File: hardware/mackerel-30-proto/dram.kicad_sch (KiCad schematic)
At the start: 8 parts, among them J11 Conn_02x05_Odd_Even, U10 SIMM72, U9 EPM7128, X3 CXO_DIP14

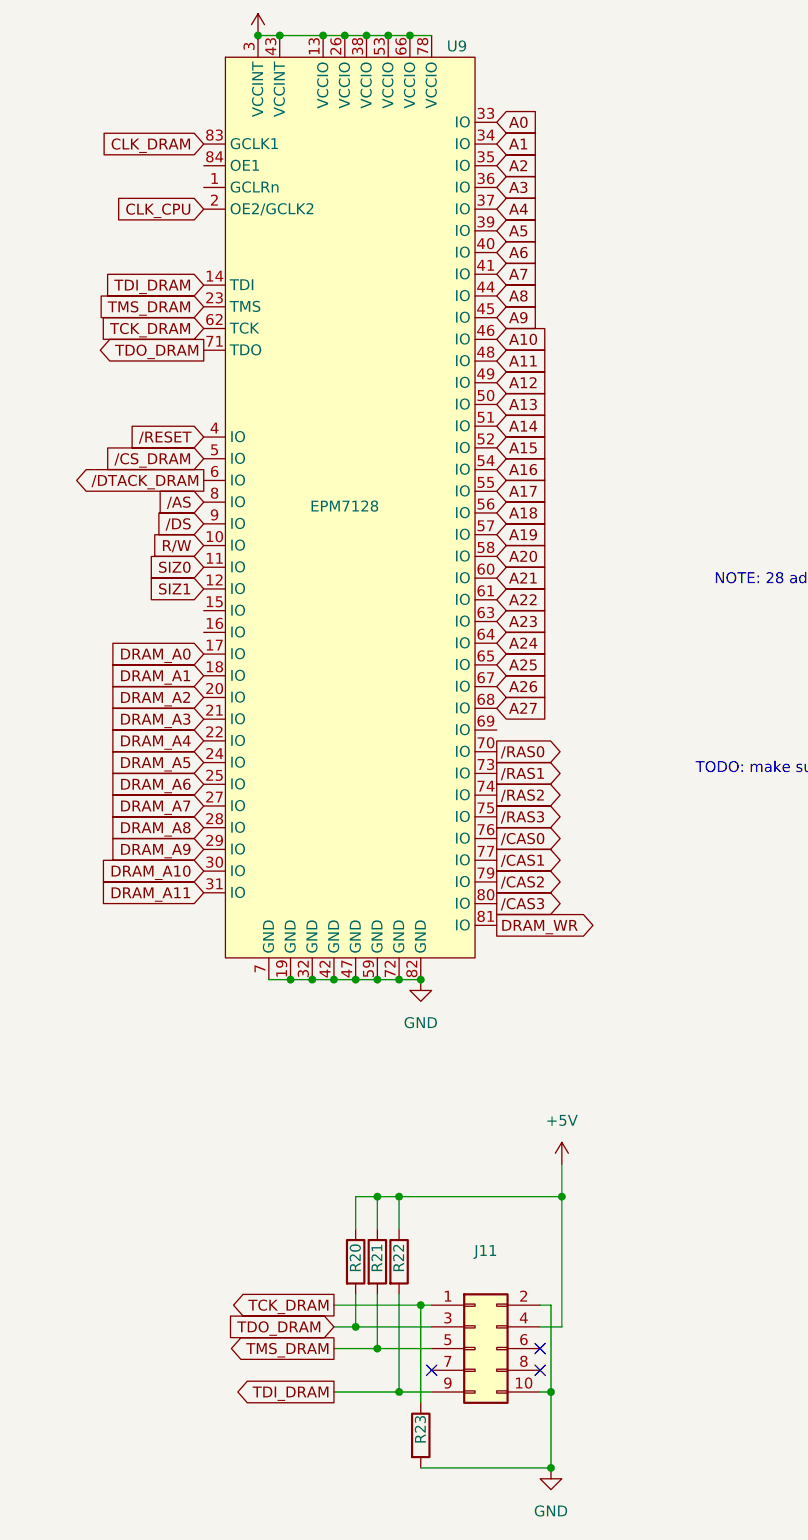
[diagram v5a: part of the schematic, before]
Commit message: rough layout of the PCB components
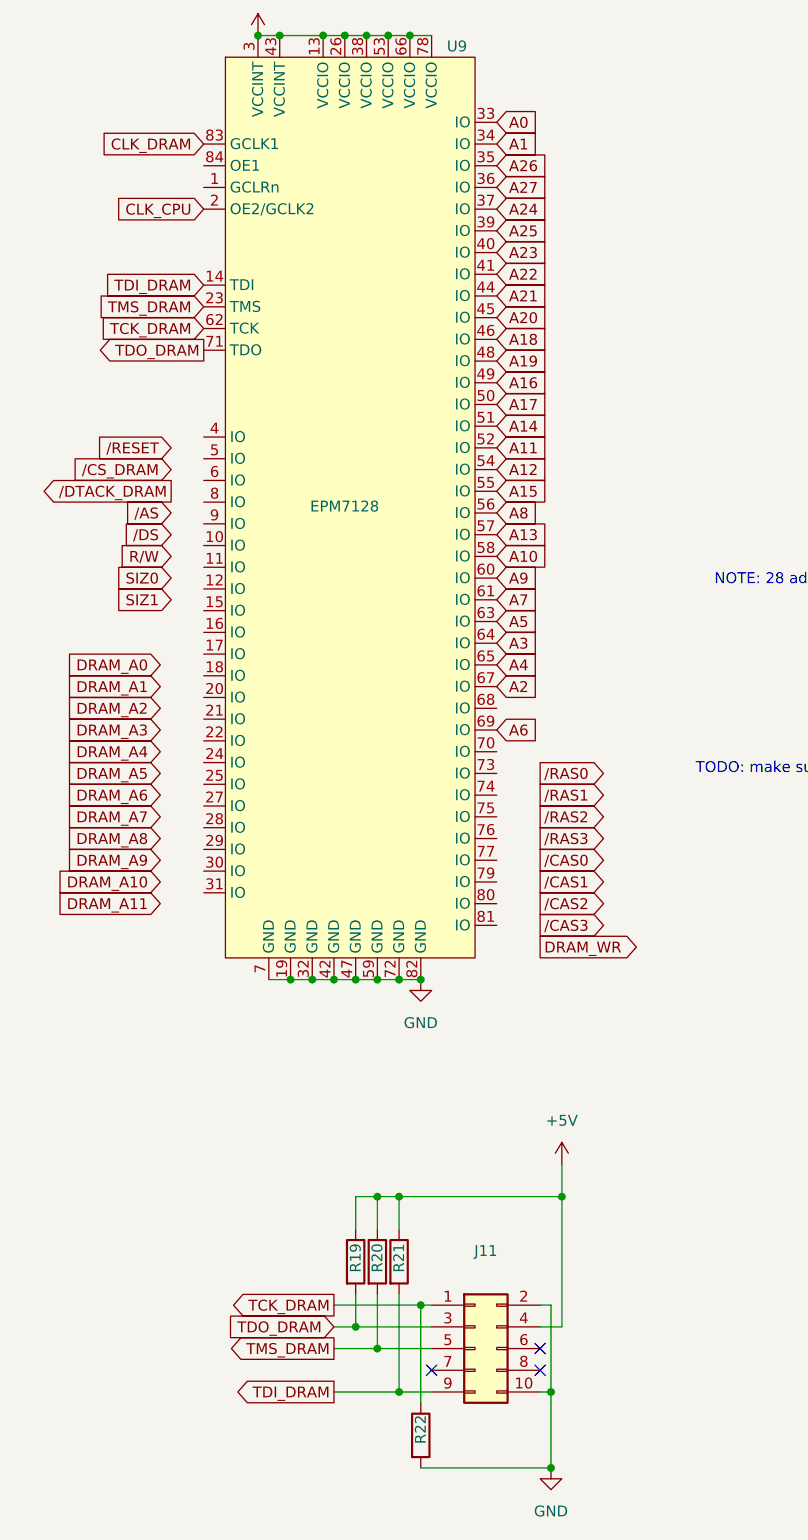
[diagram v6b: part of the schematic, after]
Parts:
- R19: renamed from R20; footprint Resistor_SMD:R_0805_2012Metric_Pad1.20x1.40mm_HandSolder -> Resistor_THT:R_Axial_DIN0207_L6.3mm_D2.5mm_P7.62mm_Horizontal
- R20: renamed from R21; footprint Resistor_SMD:R_0805_2012Metric_Pad1.20x1.40mm_HandSolder -> Resistor_THT:R_Axial_DIN0207_L6.3mm_D2.5mm_P7.62mm_Horizontal
- R21: renamed from R22; footprint Resistor_SMD:R_0805_2012Metric_Pad1.20x1.40mm_HandSolder -> Resistor_THT:R_Axial_DIN0207_L6.3mm_D2.5mm_P7.62mm_Horizontal
- R22: renamed from R23; footprint Resistor_SMD:R_0805_2012Metric_Pad1.20x1.40mm_HandSolder -> Resistor_THT:R_Axial_DIN0207_L6.3mm_D2.5mm_P7.62mm_Horizontal
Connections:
- net A10: now also U9.58 (IO); no longer U9.46 (IO)
- net A11: now also U9.52 (IO); no longer U9.48 (IO)
- net A12: now also U9.54 (IO); no longer U9.49 (IO)
- net A13: now also U9.57 (IO); no longer U9.50 (IO)
- net A15: now also U9.55 (IO); no longer U9.52 (IO)
- net A16: now also U9.49 (IO); no longer U9.54 (IO)
- net A17: now also U9.50 (IO); no longer U9.55 (IO)
- net A18: now also U9.46 (IO); no longer U9.56 (IO)
- net A19: now also U9.48 (IO); no longer U9.57 (IO)
- net A2: now also U9.67 (IO); no longer U9.35 (IO)
- net A20: now also U9.45 (IO); no longer U9.58 (IO)
- net A21: now also U9.44 (IO); no longer U9.60 (IO)
- net A22: now also U9.41 (IO); no longer U9.61 (IO)
- net A23: now also U9.40 (IO); no longer U9.63 (IO)
- net A24: now also U9.37 (IO); no longer U9.64 (IO)
- net A25: now also U9.39 (IO); no longer U9.65 (IO)
- net A26: now also U9.35 (IO); no longer U9.67 (IO)
- net A27: now also U9.36 (IO); no longer U9.68 (IO)
- net A3: now also U9.64 (IO); no longer U9.36 (IO)
- net A4: now also U9.65 (IO); no longer U9.37 (IO)
- net A5: now also U9.63 (IO); no longer U9.39 (IO)
- net A6: now also U9.69 (IO); no longer U9.40 (IO)
- net A7: now also U9.61 (IO); no longer U9.41 (IO)
- net A8: now also U9.56 (IO); no longer U9.44 (IO)
- net A9: now also U9.60 (IO); no longer U9.45 (IO)
- net DRAM_A0: no longer U9.17 (IO)
- net DRAM_A1: no longer U9.18 (IO)
- net DRAM_A10: no longer U9.30 (IO)
- net DRAM_A11: no longer U9.31 (IO)
- net DRAM_A2: no longer U9.20 (IO)
- net DRAM_A3: no longer U9.21 (IO)
- net DRAM_A4: no longer U9.22 (IO)
- net DRAM_A5: no longer U9.24 (IO)
- net DRAM_A6: no longer U9.25 (IO)
- net DRAM_A7: no longer U9.27 (IO)
- net DRAM_A8: no longer U9.28 (IO)
- net DRAM_A9: no longer U9.29 (IO)
- net DRAM_WR: no longer U9.81 (IO)
- net R/W: no longer U9.10 (IO)
- net SIZ0: no longer U9.11 (IO)
- net SIZ1: no longer U9.12 (IO)
- net /AS: no longer U9.8 (IO)
- net /CAS0: no longer U9.76 (IO)
- net /CAS1: no longer U9.77 (IO)
- net /CAS2: no longer U9.79 (IO)
- net /CAS3: no longer U9.80 (IO)
- net /CS_DRAM: no longer U9.5 (IO)
- net /DS: no longer U9.9 (IO)
- net /DTACK_DRAM: no longer U9.6 (IO)
- net /RAS0: no longer U9.70 (IO)
- net /RAS1: no longer U9.73 (IO)
- net /RAS2: no longer U9.74 (IO)
- net /RAS3: no longer U9.75 (IO)
- net /RESET: no longer U9.4 (IO)

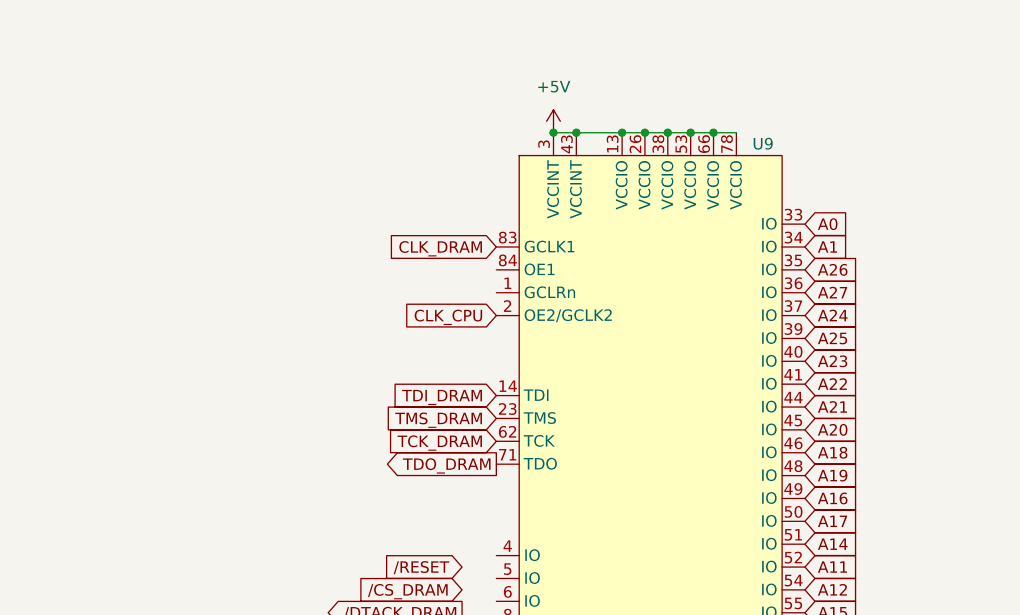
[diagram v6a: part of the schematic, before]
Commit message: Rough routing of data bus to FPU and RAM
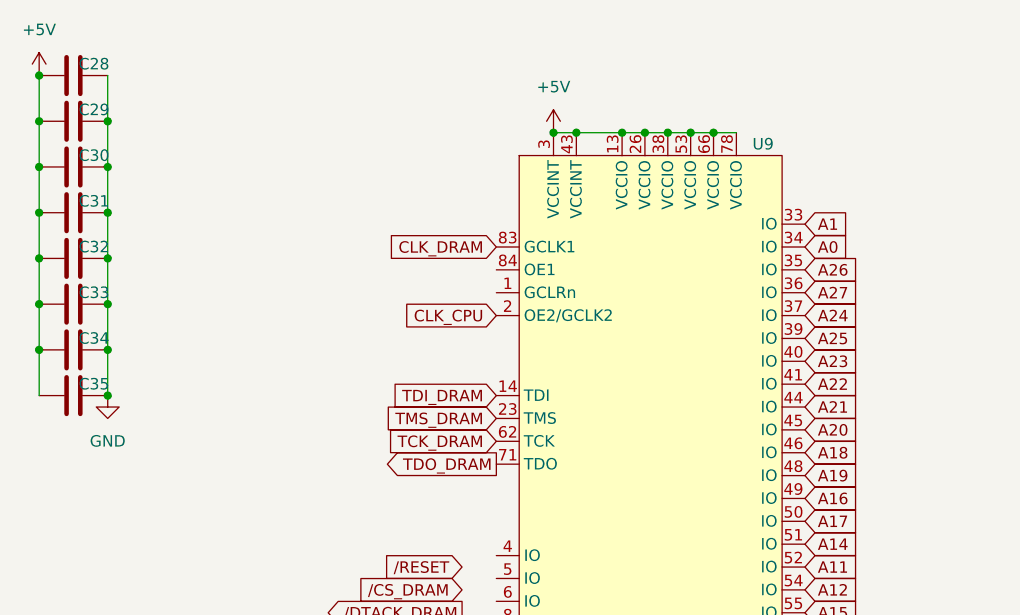
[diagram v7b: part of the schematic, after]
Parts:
- added C28, C29, C30, C31, C32, C33, C34, C35: 0.1uF, Capacitor_THT:C_Disc_D4.3mm_W1.9mm_P5.00mm, symbol Device:C
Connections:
- net +5V: now also C28.1, C29.1, C30.1, C31.1, C32.1, C33.1, C34.1, C35.1
- net A0: now also U9.34 (IO); no longer U9.33 (IO)
- net A1: now also U9.33 (IO); no longer U9.34 (IO)
- net GND: now also C28.2, C29.2, C30.2, C31.2, C32.2, C33.2, C34.2, C35.2

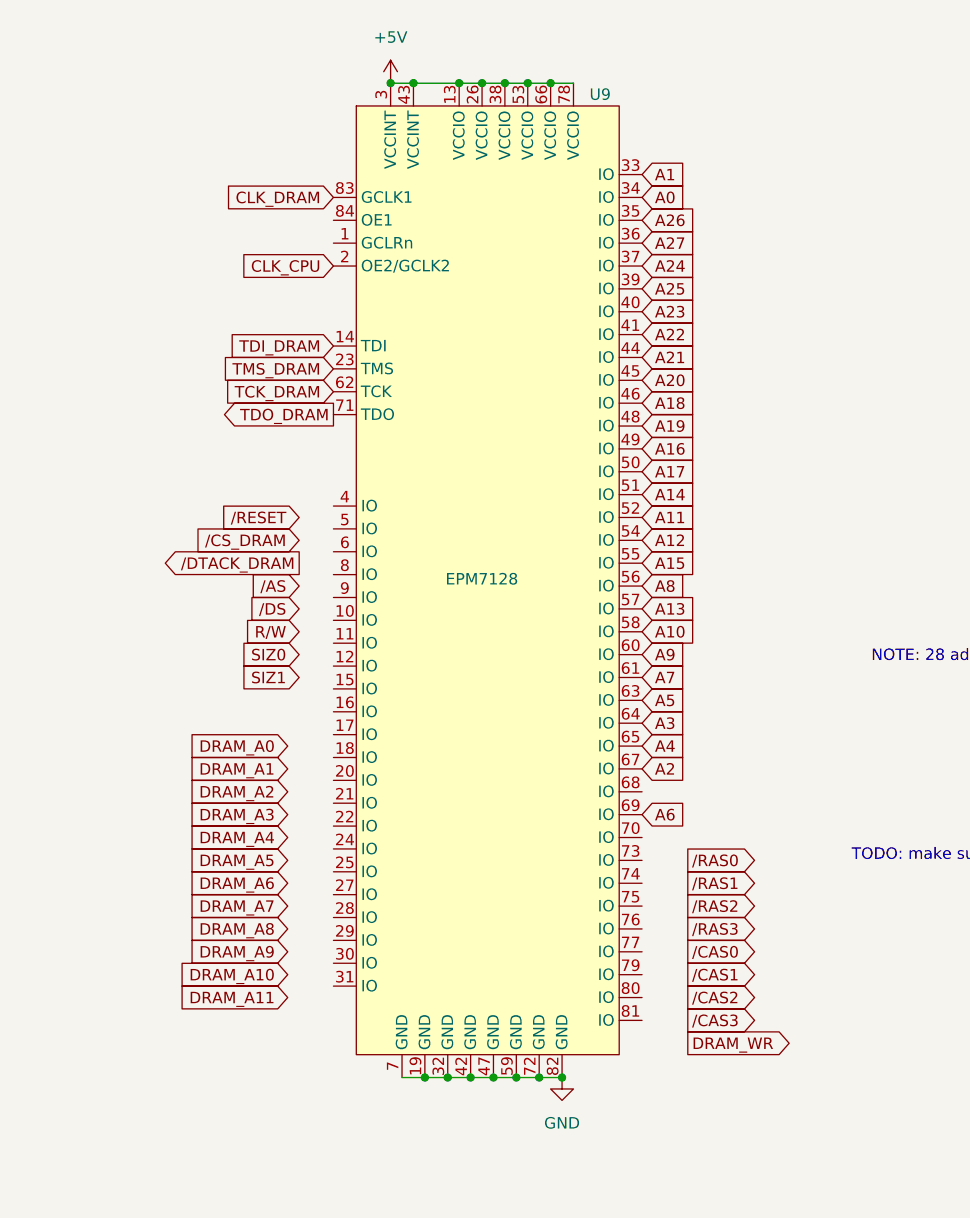
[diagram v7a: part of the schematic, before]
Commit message: DRAM mostly routed
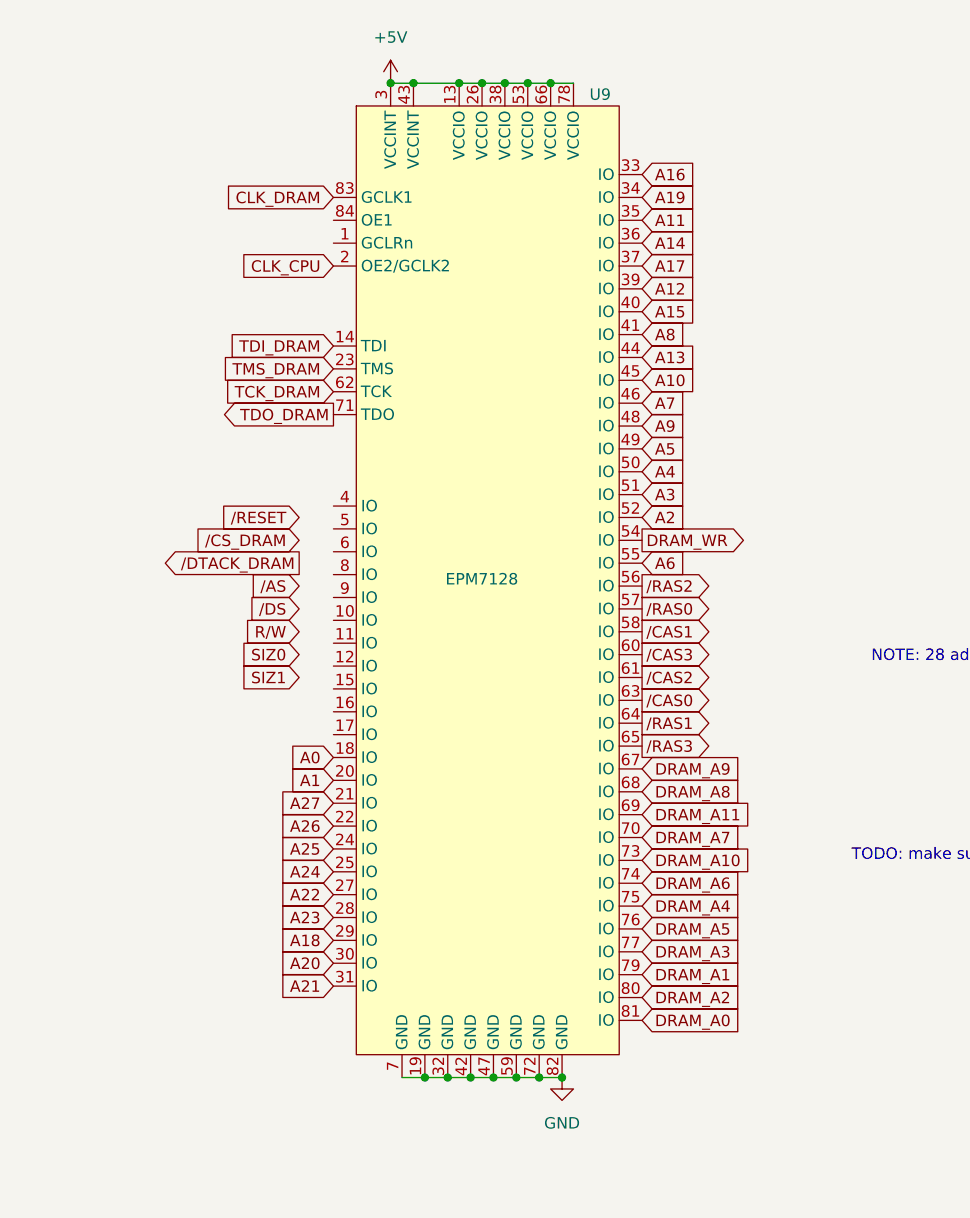
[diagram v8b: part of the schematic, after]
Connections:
- net A0: now also U9.18 (IO); no longer U9.34 (IO)
- net A1: now also U9.20 (IO); no longer U9.33 (IO)
- net A10: now also U9.45 (IO); no longer U9.58 (IO)
- net A11: now also U9.35 (IO); no longer U9.52 (IO)
- net A12: now also U9.39 (IO); no longer U9.54 (IO)
- net A13: now also U9.44 (IO); no longer U9.57 (IO)
- net A14: now also U9.36 (IO); no longer U9.51 (IO)
- net A15: now also U9.40 (IO); no longer U9.55 (IO)
- net A16: now also U9.33 (IO); no longer U9.49 (IO)
- net A17: now also U9.37 (IO); no longer U9.50 (IO)
- net A18: now also U9.29 (IO); no longer U9.46 (IO)
- net A19: now also U9.34 (IO); no longer U9.48 (IO)
- net A2: now also U9.52 (IO); no longer U9.67 (IO)
- net A20: now also U9.30 (IO); no longer U9.45 (IO)
- net A21: now also U9.31 (IO); no longer U9.44 (IO)
- net A22: now also U9.27 (IO); no longer U9.41 (IO)
- net A23: now also U9.28 (IO); no longer U9.40 (IO)
- net A24: now also U9.25 (IO); no longer U9.37 (IO)
- net A25: now also U9.24 (IO); no longer U9.39 (IO)
- net A26: now also U9.22 (IO); no longer U9.35 (IO)
- net A27: now also U9.21 (IO); no longer U9.36 (IO)
- net A3: now also U9.51 (IO); no longer U9.64 (IO)
- net A4: now also U9.50 (IO); no longer U9.65 (IO)
- net A5: now also U9.49 (IO); no longer U9.63 (IO)
- net A6: now also U9.55 (IO); no longer U9.69 (IO)
- net A7: now also U9.46 (IO); no longer U9.61 (IO)
- net A8: now also U9.41 (IO); no longer U9.56 (IO)
- net A9: now also U9.48 (IO); no longer U9.60 (IO)
- net DRAM_A0: now also U9.81 (IO)
- net DRAM_A1: now also U9.79 (IO)
- net DRAM_A10: now also U9.73 (IO)
- net DRAM_A11: now also U9.69 (IO)
- net DRAM_A2: now also U9.80 (IO)
- net DRAM_A3: now also U9.77 (IO)
- net DRAM_A4: now also U9.75 (IO)
- net DRAM_A5: now also U9.76 (IO)
- net DRAM_A6: now also U9.74 (IO)
- net DRAM_A7: now also U9.70 (IO)
- net DRAM_A8: now also U9.68 (IO)
- net DRAM_A9: now also U9.67 (IO)
- net DRAM_WR: now also U9.54 (IO)
- net /CAS0: now also U9.63 (IO)
- net /CAS1: now also U9.58 (IO)
- net /CAS2: now also U9.61 (IO)
- net /CAS3: now also U9.60 (IO)
- net /RAS0: now also U9.57 (IO)
- net /RAS1: now also U9.64 (IO)
- net /RAS2: now also U9.56 (IO)
- net /RAS3: now also U9.65 (IO)
